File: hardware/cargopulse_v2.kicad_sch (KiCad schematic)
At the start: 13 parts

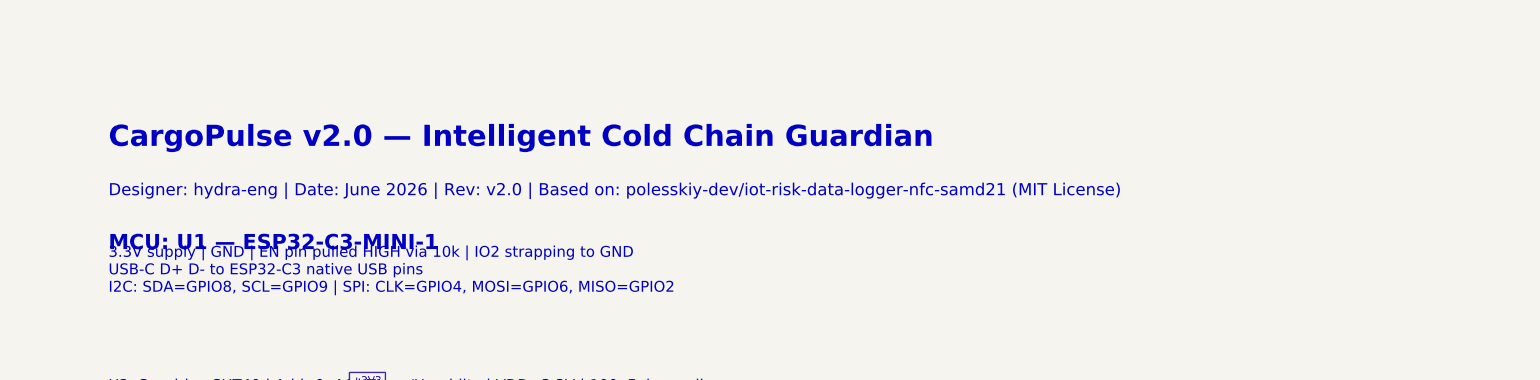
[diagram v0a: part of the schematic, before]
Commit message: refactor: overhaul readme, remove credits, remove hackathon references, remove BOM, and add visual assets
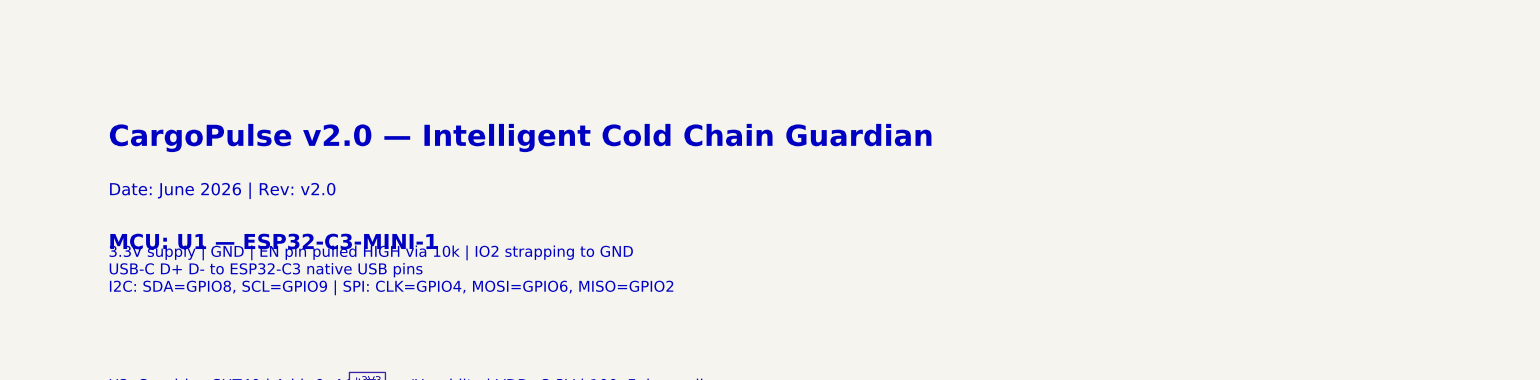
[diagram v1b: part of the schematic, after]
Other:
- note added: "Date: June 2026 | Rev: v2.0"
- note removed: "Designer: hydra-eng | Date: June 2026 | Rev: v2.0 | Based on: polesskiy-dev/iot-risk-data-logger-nfc-samd21 (MIT License)"
